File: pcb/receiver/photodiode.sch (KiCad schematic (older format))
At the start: 111 parts, among them Q201 BFR31,215, Q202 MMBT2222A-7-F, Q203 MMBT2222A-7-F, Q204 MMBT2222A-7-F, Q205 MMBT2222A-7-F, Q206 MMBT2222A-7-F, Q207 TF414T5G, U201 ADR550ARTZ-REEL7, U202 TL974IPWR, U203 MAX4477AUA+, U204 OPA2141AIDR, U205 NLAS4599DFT2G

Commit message: Finish footprinting/sourcing all components
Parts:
- C232: footprint (none) -> Capacitors_SMD:C_0402; Mouser (none) -> 710-885012005074
- R213: footprint (none) -> Resistors_SMD:R_0402; Mouser (none) -> 603-RC0402JR-13100KL
- R225: footprint (none) -> Resistors_SMD:R_0603_HandSoldering; Mouser (none) -> 603-RC0603FR-1012KL
- R246: footprint (none) -> Resistors_SMD:R_0603_HandSoldering; Mouser (none) -> 603-RC0603JR-071KL
- R247: footprint (none) -> Resistors_SMD:R_0603_HandSoldering; Mouser (none) -> 603-RC0603FR-0710KL
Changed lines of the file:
@@
 F 0 "R225" H 7230 2320 50  0000 L CNN
 F 1 "12k" H 7230 2260 50  0000 L CNN
-F 2 "" H 7200 2300 50  0001 C CNN
+F 2 "Resistors_SMD:R_0603_HandSoldering" H 7200 2300 50  0001 C CNN
 F 3 "~" H 7200 2300 50  0001 C CNN
+F 4 "603-RC0603FR-1012KL" H 7200 2300 50  0001 C CNN "Mouser"
 	1    7200 2300
 	-1   0    0    -1
@@
 F 0 "C232" H 9310 1670 50  0000 L CNN
 F 1 "10 pF" H 9310 1520 50  0000 L CNN
-F 2 "" H 9300 1600 50  0001 C CNN
+F 2 "Capacitors_SMD:C_0402" H 9300 1600 50  0001 C CNN
 F 3 "~" H 9300 1600 50  0001 C CNN
+F 4 "710-885012005074" H 9300 1600 50  0001 C CNN "Mouser"
 	1    9300 1600
 	0    -1   -1   0
@@
 F 0 "R213" H 4380 3820 50  0000 L CNN
 F 1 "100k" H 4380 3760 50  0000 L CNN
-F 2 "" H 4350 3800 50  0001 C CNN
+F 2 "Resistors_SMD:R_0402" H 4350 3800 50  0001 C CNN
 F 3 "~" H 4350 3800 50  0001 C CNN
+F 4 "603-RC0402JR-13100KL" H 4350 3800 50  0001 C CNN "Mouser"
 	1    4350 3800
 	1    0    0    -1
@@
 F 0 "R246" H 2780 6170 50  0000 L CNN
 F 1 "1k" H 2780 6110 50  0000 L CNN
-F 2 "" H 2750 6150 50  0001 C CNN
+F 2 "Resistors_SMD:R_0603_HandSoldering" H 2750 6150 50  0001 C CNN
 F 3 "~" H 2750 6150 50  0001 C CNN
+F 4 "603-RC0603JR-071KL" H 2750 6150 50  0001 C CNN "Mouser"
 	1    2750 6150
 	1    0    0    -1
@@
 F 0 "R247" H 6280 5520 50  0000 L CNN
 F 1 "10k" H 6280 5460 50  0000 L CNN
-F 2 "" H 6250 5500 50  0001 C CNN
+F 2 "Resistors_SMD:R_0603_HandSoldering" H 6250 5500 50  0001 C CNN
 F 3 "~" H 6250 5500 50  0001 C CNN
+F 4 "603-RC0603FR-0710KL" H 6250 5500 50  0001 C CNN "Mouser"
 	1    6250 5500
 	1    0    0    -1

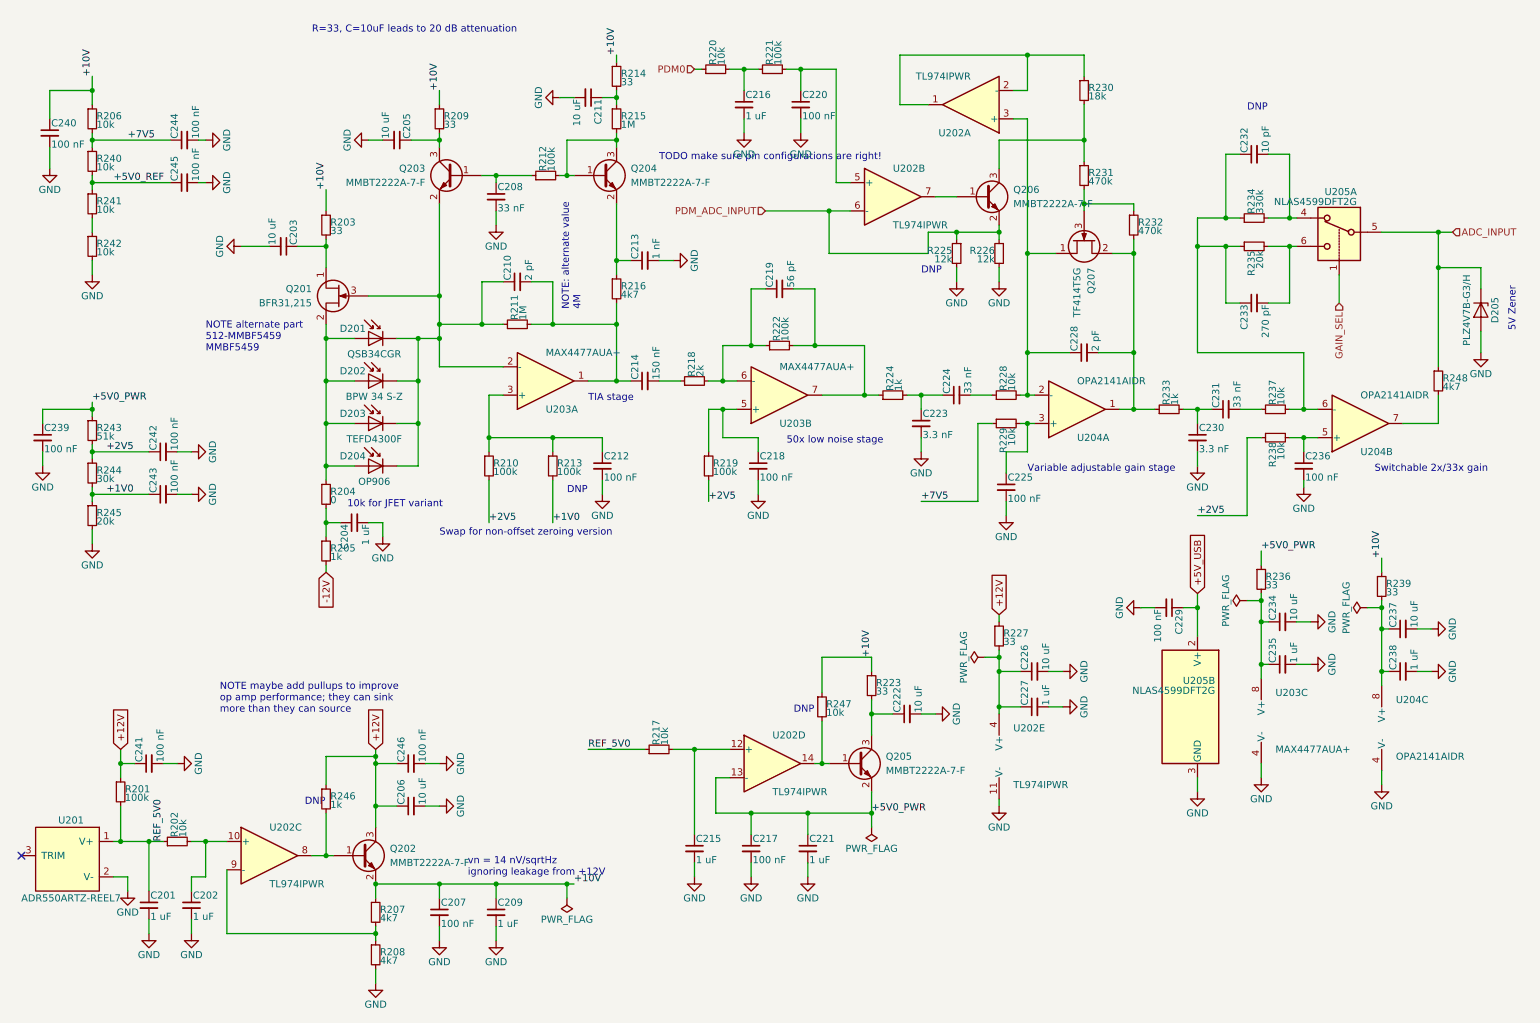
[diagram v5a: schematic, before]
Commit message: Most of the layout done TODO add test points for +12V, AVR_UART, various amplifier stage outputs
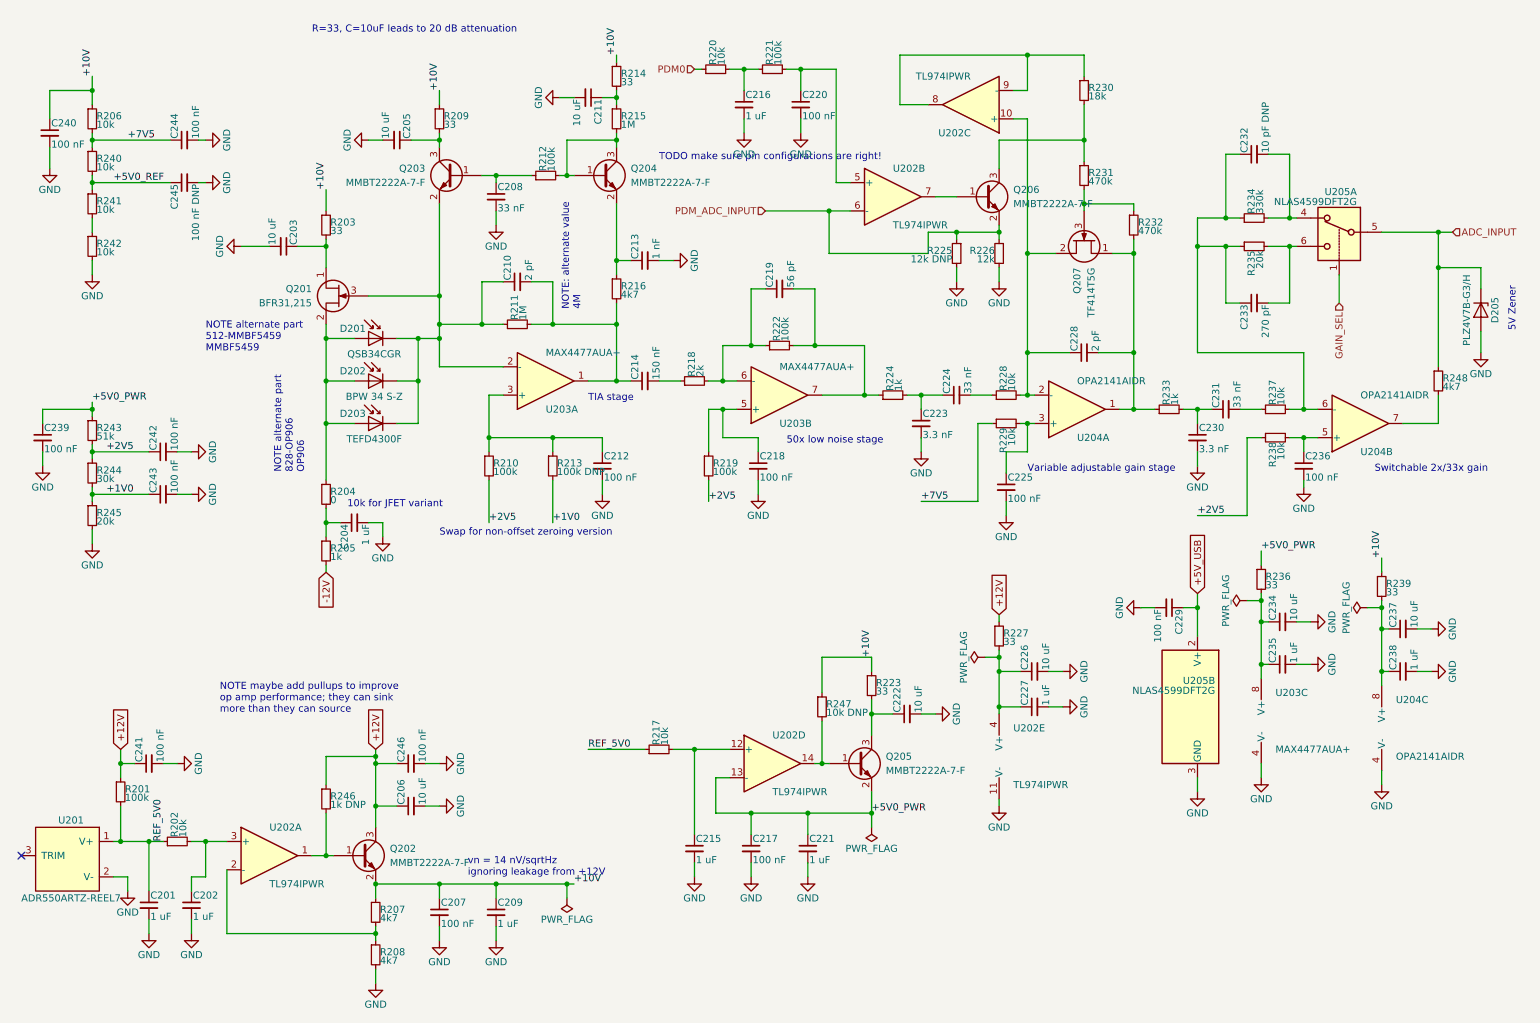
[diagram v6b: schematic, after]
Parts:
- removed D204: OP906, LEDs:LED_D3.0mm, symbol Device:D_Photo
- C232: value 10 pF -> 10 pF DNP
- C245: value 100 nF -> 100 nF DNP
- R213: value 100k -> 100k DNP
- R225: value 12k -> 12k DNP
- R246: value 1k -> 1k DNP
- R247: value 10k -> 10k DNP
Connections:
- net at C228.2, R232.2, R233.1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: now also Q207.1 (S); no longer Q207.2 (D)
- net at C228.1, R228.2, U204.2 (-): now also Q207.2 (D), U202.10 (+); no longer Q207.1 (S), U202.3 (+)
- net at C202.1, R202.2: now also U202.3 (+); no longer U202.10 (+)
- net at Q202.1 (B), R246.2: now also U202.1; no longer U202.8
- net at R207.2, R208.1: now also U202.2 (-); no longer U202.9 (-)
- new net: R230.1, U202.8, U202.9 (-)
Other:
- note added: "NOTE alternate part\n828-OP906\nOP906"
- note removed: "DNP"
- moved on the sheet: U202A, U202C
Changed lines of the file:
@@
-	-1   0    0    -1
-$EndComp
-$Comp
-L Device:D_Photo D204
-U 1 1 5C072B7E
-P 3050 3800
-F 0 "D204" H 3070 3870 50  0000 L CNN
-F 1 "OP906" H 3010 3690 50  0000 C CNN
-F 2 "LEDs:LED_D3.0mm" H 3000 3800 50  0001 C CNN
-F 3 "~" H 3000 3800 50  0001 C CNN
-F 4 "828-OP906" H 3050 3800 50  0001 C CNN "Mouser"
-	1    3050 3800
 	-1   0    0    -1
 $EndComp
@@
 	3400 3500 3250 3500
 Connection ~ 3400 3200
-Wire Wire Line
-	2750 3500 2750 3800
-Wire Wire Line
-	2750 3800 2950 3800
 Connection ~ 2750 3500
-Wire Wire Line
-	3400 3500 3400 3800
-Wire Wire Line
-	3400 3800 3250 3800
-Connection ~ 3400 3500
 $Comp
 L Device:R_Small R204
@@
 Text Notes 2900 4100 0    50   ~ 0
 10k for JFET variant
-Wire Wire Line
-	2750 3800 2750 3900
-Connection ~ 2750 3800
 Wire Wire Line
 	3050 2600 3550 2600
@@
 L receiver:TL974IPWR U202
 U 1 1 5C072C4C
-P 7300 1250
-F 0 "U202" H 7300 1450 50  0000 L CNN
-F 1 "TL974IPWR" H 7300 1050 50  0000 L CNN
-F 2 "receiver-footprints:TI-SOIC14" H 7250 1350 50  0001 C CNN
-F 3 "" H 7350 1450 50  0001 C CNN
-F 4 "595-TL974IPWR" H 7350 1450 50  0001 C CNN "Mouser"
-	1    7300 1250
-	-1   0    0    1
+P 2350 6550
+F 0 "U202" H 2350 6750 50  0000 L CNN
+F 1 "TL974IPWR" H 2350 6350 50  0000 L CNN
+F 2 "receiver-footprints:TI-SOIC14" H 2300 6650 50  0001 C CNN
+F 3 "" H 2400 6750 50  0001 C CNN
+F 4 "595-TL974IPWR" H 2400 6750 50  0001 C CNN "Mouser"
+	1    2350 6550
+	1    0    0    -1
 $EndComp
 $Comp
@@
 P 7200 2300
 F 0 "R225" H 7230 2320 50  0000 L CNN
-F 1 "12k" H 7230 2260 50  0000 L CNN
+F 1 "12k DNP" H 7230 2260 50  0000 L CNN
 F 2 "Resistors_SMD:R_0603_HandSoldering" H 7200 2300 50  0001 C CNN
 F 3 "~" H 7200 2300 50  0001 C CNN
@@
 P 9300 1600
 F 0 "C232" H 9310 1670 50  0000 L CNN
-F 1 "10 pF" H 9310 1520 50  0000 L CNN
+F 1 "10 pF DNP" H 9310 1520 50  0000 L CNN
 F 2 "Capacitors_SMD:C_0402" H 9300 1600 50  0001 C CNN
 F 3 "~" H 9300 1600 50  0001 C CNN
@@
 P 4350 3800
 F 0 "R213" H 4380 3820 50  0000 L CNN
-F 1 "100k" H 4380 3760 50  0000 L CNN
+F 1 "100k DNP" H 4380 3760 50  0000 L CNN
 F 2 "Resistors_SMD:R_0402" H 4350 3800 50  0001 C CNN
 F 3 "~" H 4350 3800 50  0001 C CNN
@@
 L receiver:TL974IPWR U?
 U 3 1 5C07D519
-P 2350 6550
+P 7300 1250
 AR Path="/5C07D519" Ref="U?"  Part="3"
 AR Path="/5C071C62/5C07D519" Ref="U202"  Part="3"
-F 0 "U202" H 2350 6750 50  0000 L CNN
-F 1 "TL974IPWR" H 2350 6350 50  0000 L CNN
-F 2 "receiver-footprints:TI-SOIC14" H 2300 6650 50  0001 C CNN
-F 3 "" H 2400 6750 50  0001 C CNN
-F 4 "595-TL974IPWR" H 2400 6750 50  0001 C CNN "Mouser"
-	3    2350 6550
-	1    0    0    -1
+F 0 "U202" H 7300 1450 50  0000 L CNN
+F 1 "TL974IPWR" H 7300 1050 50  0000 L CNN
+F 2 "receiver-footprints:TI-SOIC14" H 7250 1350 50  0001 C CNN
+F 3 "" H 7350 1450 50  0001 C CNN
+F 4 "595-TL974IPWR" H 7350 1450 50  0001 C CNN "Mouser"
+	3    7300 1250
+	-1   0    0    1
 $EndComp
 Wire Wire Line
@@
 P 1750 1800
 F 0 "C245" H 1760 1870 50  0000 L CNN
-F 1 "100 nF" H 1760 1720 50  0000 L CNN
+F 1 "100 nF DNP" H 1760 1720 50  0000 L CNN
 F 2 "Capacitors_SMD:C_0603_HandSoldering" H 1750 1800 50  0001 C CNN
 F 3 "~" H 1750 1800 50  0001 C CNN
 F 4 "710-885012206071" H 1750 1800 50  0001 C CNN "Mouser"
 	1    1750 1800
-	0    -1   -1   0
+	0    -1   1    0
 $EndComp
 $Comp
@@
 P 2750 6150
 F 0 "R246" H 2780 6170 50  0000 L CNN
-F 1 "1k" H 2780 6110 50  0000 L CNN
+F 1 "1k DNP" H 2780 6110 50  0000 L CNN
 F 2 "Resistors_SMD:R_0603_HandSoldering" H 2750 6150 50  0001 C CNN
 F 3 "~" H 2750 6150 50  0001 C CNN
@@
 P 6250 5500
 F 0 "R247" H 6280 5520 50  0000 L CNN
-F 1 "10k" H 6280 5460 50  0000 L CNN
+F 1 "10k DNP" H 6280 5460 50  0000 L CNN
 F 2 "Resistors_SMD:R_0603_HandSoldering" H 6250 5500 50  0001 C CNN
 F 3 "~" H 6250 5500 50  0001 C CNN
@@
 F 4 "863-TF414T5G" H 8100 2200 50  0001 C CNN "Mouser"
 	1    8100 2200
-	0    1    1    0
+	0    -1   1    0
 $EndComp
 Text Notes 1900 3000 0    50   ~ 0
@@
 Text Notes 4550 2700 1    50   ~ 0
 NOTE: alternate value\n4M
-Text Notes 6950 2450 0    50   ~ 0
-DNP
-Text Notes 9250 1300 0    50   ~ 0
-DNP
-Text Notes 4450 4000 0    50   ~ 0
-DNP
-Text Notes 2600 6200 0    50   ~ 0
-DNP
-Text Notes 6050 5550 0    50   ~ 0
-DNP
+Text Notes 2600 3850 1    50   ~ 0
+NOTE alternate part\n828-OP906\nOP906
+Wire Wire Line
+	2750 3500 2750 3900
 $EndSCHEMATC
